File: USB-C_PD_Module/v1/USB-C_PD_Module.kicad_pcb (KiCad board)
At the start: 4 copper layers, 35.6 x 20.3 mm, 22 parts, among them J1 USB_C_Receptacle_USB2.0_16P, J2 Conn_01x10, J3 Conn_01x10, Q1 IRF7328TRPBF, U1 TPD4E02B04DQA, U2 TVS2200DRV, U3 TVS2200DRV, U4 CYPD3177-24LQ

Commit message: Changed file structure and finalized PCB
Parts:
- added G***: LOGO, LOGO, F.Cu at (121.9, 104.6)
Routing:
- net GND: vias 61 -> 55
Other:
- board text added: "D+"
- board text added: "D-"
- board text added: "FAULT"
- board text added: "FLIP"
- board text added: "GND"
- board text added: "ISNK_COARSE"
- board text added: "ISNK_FINE"
- board text added: "PWR OK"
- board text added: "VBOUS OUT"
- board text added: "VBUS_MAX"
- board text added: "VBUS_MIN"

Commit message: First Panel
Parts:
- moved C2 33.1 mm to (169.4, 102.4)
- moved C5 33.1 mm to (157.7, 114.7)
- moved R1 33.1 mm to (153.1, 102.4)
- moved R2 33.1 mm to (146.1, 102.4)
- moved R4 33.1 mm to (170.1, 115.1)
- moved R6 33.1 mm to (172.0, 115.1)
- moved C1 33.1 mm to (169.4, 107.5)
- moved C3 33.1 mm to (169.4, 105.0)
- moved C4 33.1 mm to (160.5, 106.9)
- moved J3 33.1 mm to (147.0, 99.4)
- moved Q1 33.1 mm to (162.5, 114.5)
- moved R5 33.1 mm to (170.8, 111.9)
- moved U1 33.1 mm to (150.6, 109.6)
- moved U2 33.1 mm to (150.8, 112.9)
- moved U3 33.1 mm to (150.8, 106.1)
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
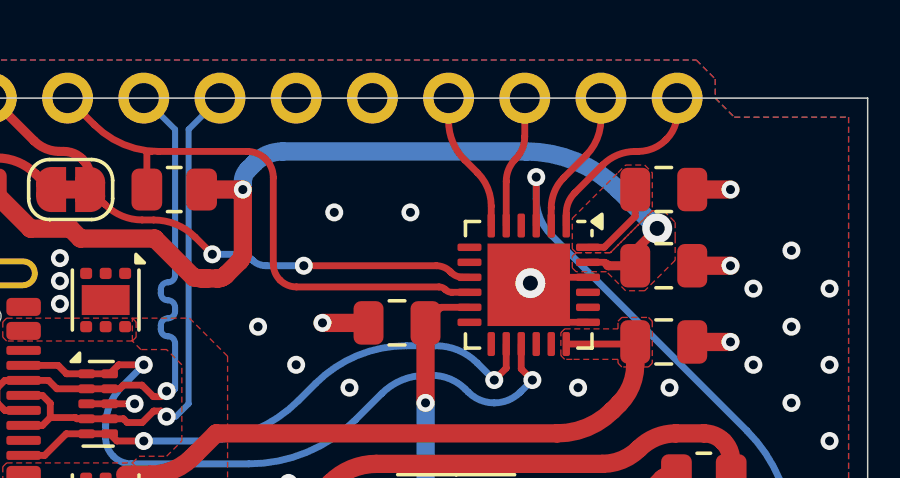
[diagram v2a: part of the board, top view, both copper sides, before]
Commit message: withouut panel
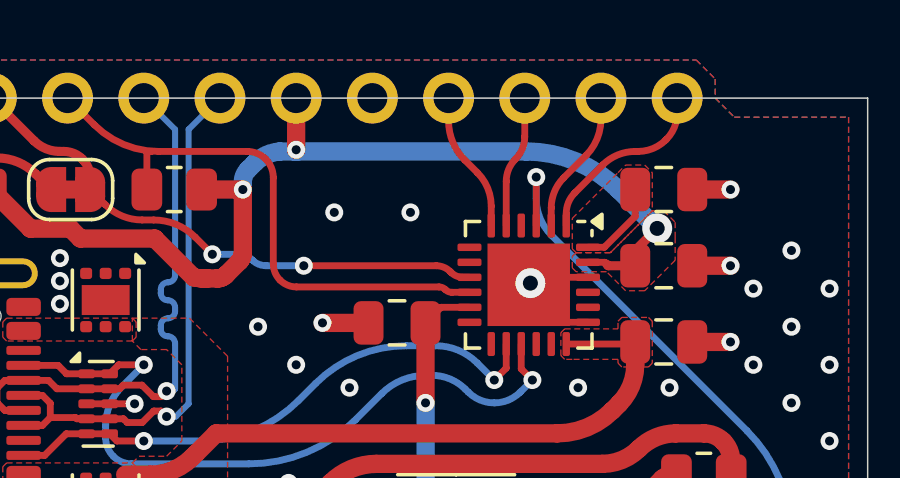
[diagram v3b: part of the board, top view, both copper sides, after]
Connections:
- J3 pad 5: GND -> +3V3
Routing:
- net +3V3: track 32.1 -> 33.8 mm, vias 2 -> 3
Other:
- board text added: "VDDD"
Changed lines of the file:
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@@
 			(layers "*.Cu" "*.Mask")
 			(remove_unused_layers no)
-			(net 4 "GND")
+			(net 23 "+3V3")
 			(pinfunction "Pin_5")
 			(pintype "passive")
@@
 	)
 	(gr_line
-		(start 158.4396 101.910401)
-		(end 159.0746 101.910401)
-		(stroke
-			(width 0.1)
-			(type default)
-		)
-		(layer "B.SilkS")
-	)
-	(gr_line
-		(start 157.1696 101.275401)
-		(end 157.8046 101.910401)
-		(stroke
-			(width 0.1)
-			(type default)
-		)
-		(layer "B.SilkS")
-	)
-	(gr_line
 		(start 159.7096 117.785401)
 		(end 160.3446 117.150401)
@@
 	)
 	(gr_line
-		(start 157.1696 100.640401)
-		(end 157.1696 101.275401)
-		(stroke
-			(width 0.1)
-			(type default)
-		)
-		(layer "B.SilkS")
-	)
-	(gr_line
 		(start 167.9646 117.150401)
 		(end 169.2346 117.150401)
@@
 	)
 	(gr_line
-		(start 157.8046 101.910401)
-		(end 158.4396 101.910401)
-		(stroke
-			(width 0.1)
-			(type default)
-		)
-		(layer "B.SilkS")
-	)
-	(gr_line
 		(start 152.0896 117.785401)
 		(end 152.7246 117.150401)
@@
 		)
 	)
+	(gr_text "VDDD"
+		(at 157.226 100.640401 270)
+		(layer "B.SilkS")
+		(effects
+			(font
+				(size 0.75 0.75)
+				(thickness 0.15)
+				(bold yes)
+			)
+			(justify right mirror)
+		)
+	)
 	(gr_text "D-"
 		(at 152.0896 100.640401 270)
@@
 	)
 	(segment
+		(start 157.1696 101.091987)
+		(end 157.169593 101.091994)
+		(width 0.6096)
+		(layer "F.Cu")
+		(net 23)
+	)
+	(segment
+		(start 157.1696 99.370401)
+		(end 157.1696 101.091987)
+		(width 0.6096)
+		(layer "F.Cu")
+		(net 23)
+	)
+	(segment
 		(start 154.58864 105.381961)
 		(end 154.532654 105.382212)
@@
 		(net 23)
 	)
+	(via
+		(at 157.169593 101.091994)
+		(size 0.6)
+		(drill 0.3)
+		(layers "F.Cu" "B.Cu")
+		(net 23)
+	)
 	(segment
-		(start 155.781473 101.538274)
-		(end 155.56493 101.754817)
+		(start 157.226 101.148401)
+		(end 157.169593 101.091994)
 		(width 0.6096)
 		(layer "B.Cu")
@@
 	)
 	(segment
-		(start 167.921127 102.431194)
-		(end 169.203921 103.713988)
+		(start 157.111733 101.149854)
+		(end 157.169593 101.091994)
 		(width 0.6096)
 		(layer "B.Cu")
@@
 	)
 	(segment
-		(start 156.722711 101.148401)
-		(end 164.82419 101.148401)
+		(start 164.82419 101.148401)
+		(end 157.226 101.148401)
 		(width 0.6096)
 		(layer "B.Cu")
@@
 	)
 	(segment
-		(start 155.3916 102.173274)
-		(end 155.3916 102.418401)
+		(start 169.203921 103.713988)
+		(end 167.921127 102.431194)
+		(width 0.6096)
+		(layer "B.Cu")
+		(net 23)
+	)
+	(segment
+		(start 156.618065 101.149854)
+		(end 157.111733 101.149854)
+		(width 0.6096)
+		(layer "B.Cu")
+		(net 23)
+	)
+	(segment
+		(start 155.56493 101.754817)
+		(end 155.781473 101.538274)
+		(width 0.6096)
+		(layer "B.Cu")
+		(net 23)
+	)
+	(segment
+		(start 155.3916 102.418401)
+		(end 155.3916 102.173274)
 		(width 0.6096)
 		(layer "B.Cu")
@@
 	)
 	(arc
-		(start 156.722711 101.148401)
-		(mid 156.213316 101.249725)
-		(end 155.781473 101.538274)
+		(start 155.781473 101.538274)
+		(mid 156.165428 101.270673)
+		(end 156.618065 101.149854)
 		(width 0.6096)
 		(layer "B.Cu")
@@
 	)
 	(arc
-		(start 155.56493 101.754817)
+		(start 155.3916 102.173274)
 		(mid 155.436646 101.946806)
-		(end 155.3916 102.173274)
+		(end 155.56493 101.754817)
 		(width 0.6096)
 		(layer "B.Cu")
